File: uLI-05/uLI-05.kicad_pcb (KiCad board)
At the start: 2 copper layers, 58 x 39.5 mm, 54 parts, among them J1 STL1550, J2 USB_B, J3 RJ25, J4 RJ25, J5 PROG, Q1 IRF7306, U1 LM78M05_TO252, U2 PC817, U3 PC817, U4 PIC18F14K50-EP, U5 ADM2483xRW, U6 USBLC6-2SC6, Y1 12MHz

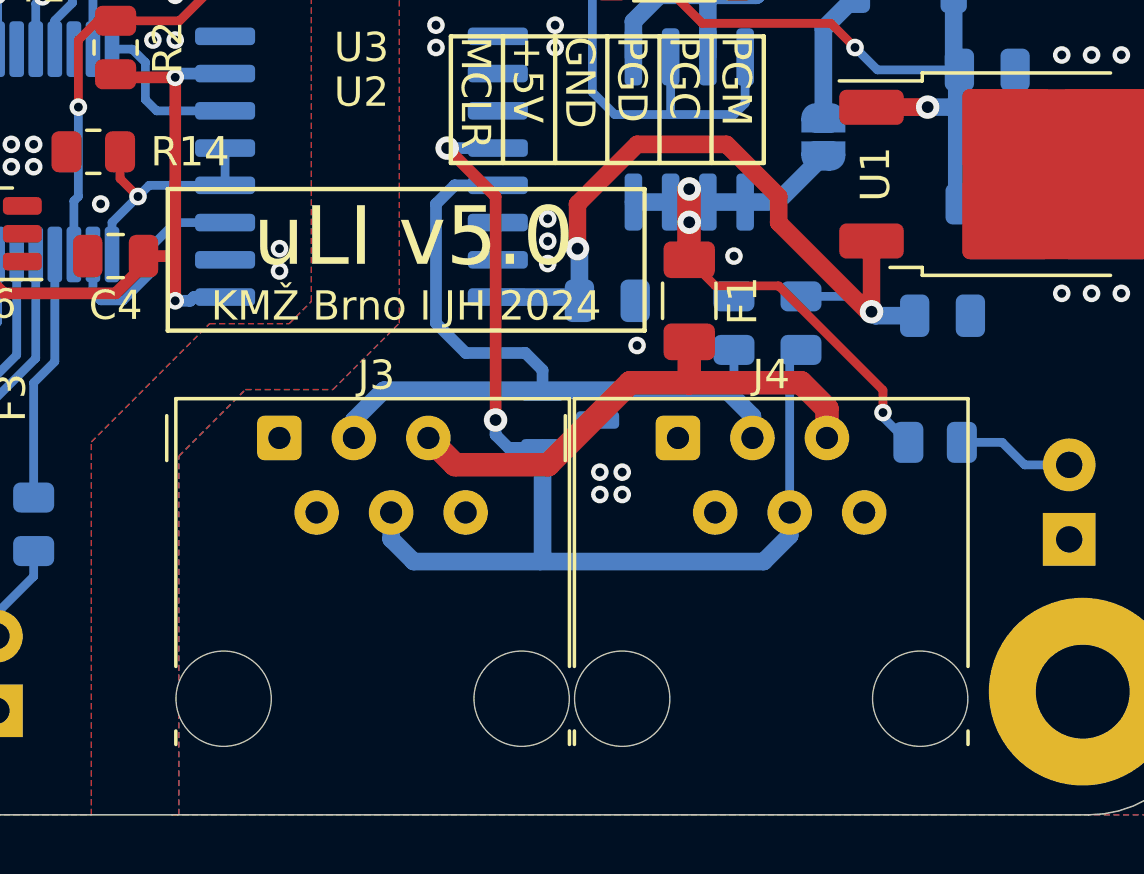
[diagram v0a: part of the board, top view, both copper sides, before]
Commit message: Use 3.0 drills for RJ12 connectors.
So the RJ12 connectors fit into the holes more precisely.
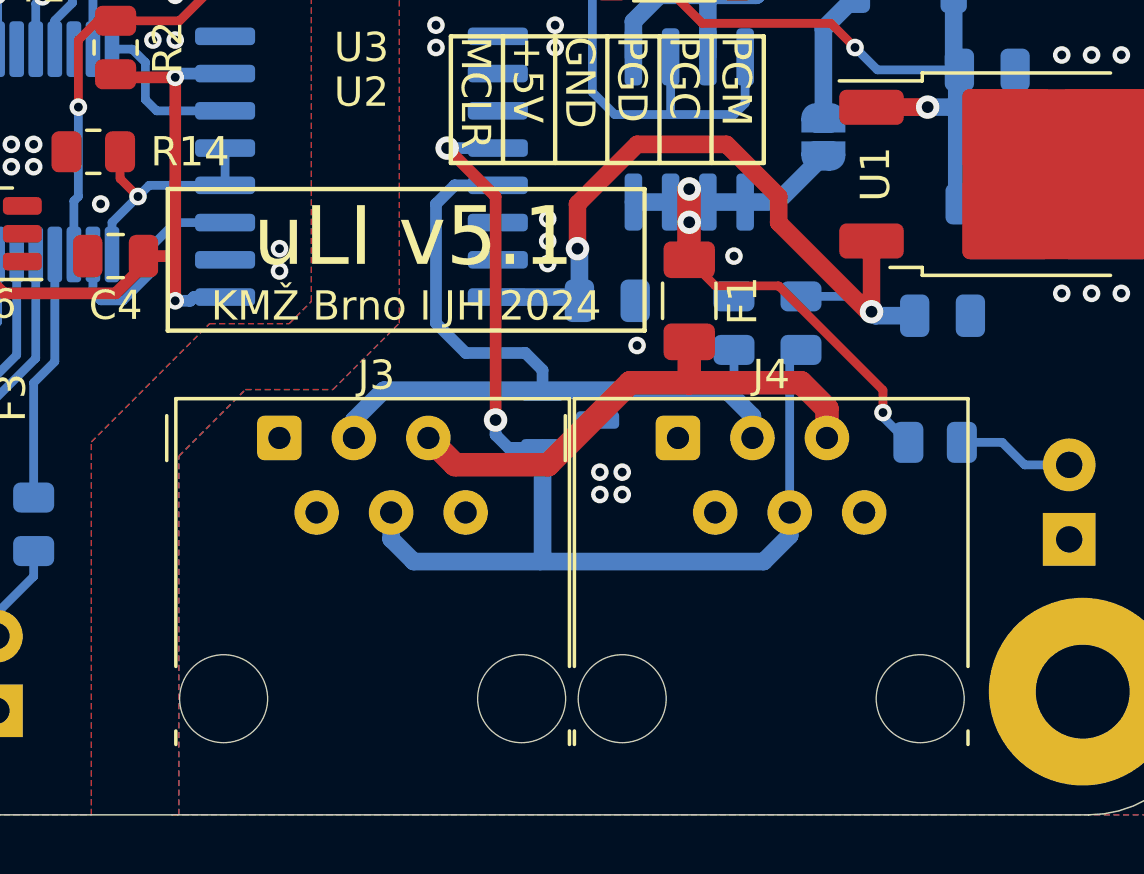
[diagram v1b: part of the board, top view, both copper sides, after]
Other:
- board text added: "uLI v5.1"
- board text removed: "uLI v5.0"
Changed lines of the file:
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@@
     (fp_line (start 9.78 16.77) (end -3.42 16.77)
       (stroke (width 0.1) (type solid)) (layer "F.Fab"))
-    (pad "" np_thru_hole circle (at -1.9 8.89) (size 3.25 3.25) (drill 3.25) (layers "*.Cu" "*.Mask"))
-    (pad "" np_thru_hole circle (at 8.26 8.89) (size 3.25 3.25) (drill 3.25) (layers "*.Cu" "*.Mask"))
+    (pad "" np_thru_hole circle (at -1.9 8.89) (size 3 3) (drill 3) (layers "F&B.Cu" "*.Mask"))
+    (pad "" np_thru_hole circle (at 8.26 8.89) (size 3 3) (drill 3) (layers "F&B.Cu" "*.Mask"))
     (pad "1" thru_hole roundrect (at 0 0) (size 1.52 1.52) (drill 0.76) (layers "*.Cu" "*.Mask") (roundrect_rratio 0.1644736842)
       (net 25 "unconnected-(J4-Pad1)") (pintype "passive+no_connect"))
@@
     (fp_line (start 9.78 16.77) (end -3.42 16.77)
       (stroke (width 0.1) (type solid)) (layer "F.Fab"))
-    (pad "" np_thru_hole circle (at -1.9 8.89) (size 3.25 3.25) (drill 3.25) (layers "*.Cu" "*.Mask"))
-    (pad "" np_thru_hole circle (at 8.26 8.89) (size 3.25 3.25) (drill 3.25) (layers "*.Cu" "*.Mask"))
+    (pad "" np_thru_hole circle (at -1.9 8.89) (size 3 3) (drill 3) (layers "F&B.Cu" "*.Mask"))
+    (pad "" np_thru_hole circle (at 8.26 8.89) (size 3 3) (drill 3) (layers "F&B.Cu" "*.Mask"))
     (pad "1" thru_hole roundrect (at 0 0) (size 1.52 1.52) (drill 0.76) (layers "*.Cu" "*.Mask") (roundrect_rratio 0.1644736842)
       (net 22 "unconnected-(J3-Pad1)") (pintype "passive+no_connect"))
@@
     (effects (font (size 1 1) (thickness 0.15)) (justify left bottom))
   )
-  (gr_text "uLI v5.0" (at 157.364 103.396) (layer "F.SilkS")
+  (gr_text "uLI v5.1" (at 157.364 103.396) (layer "F.SilkS")
     (effects (font (size 2 2) (thickness 0.25)) (justify bottom))
   )
